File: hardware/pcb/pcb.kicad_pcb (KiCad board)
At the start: 2 copper layers, 26.7 x 56.6 mm, 32 parts, among them J1 L_GPIO, J2 R_GPIO, J3 USB_C_Receptacle_USB2.0_14P, U1 ESP32-C3-WROOM-02, U3 TPS62291

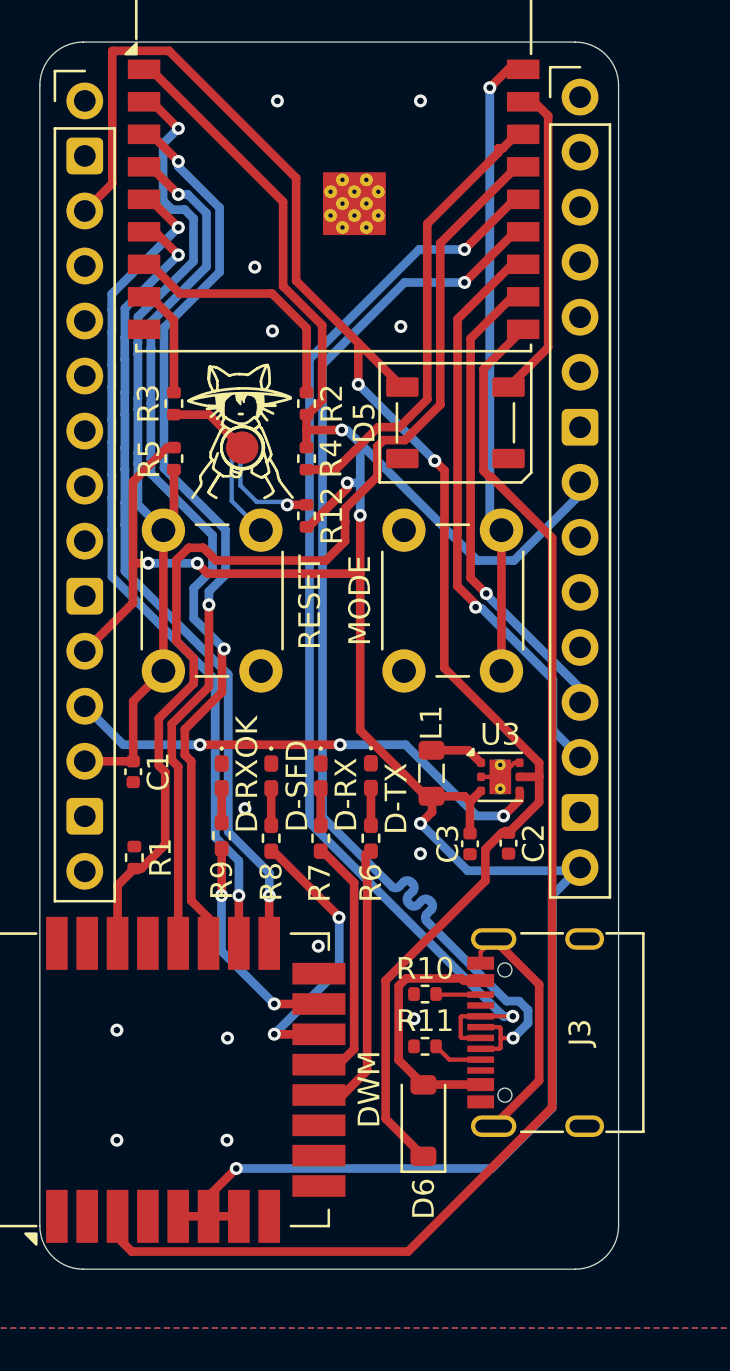
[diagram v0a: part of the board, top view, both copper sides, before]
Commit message: PCB: add some silkscreen art and transparency edits
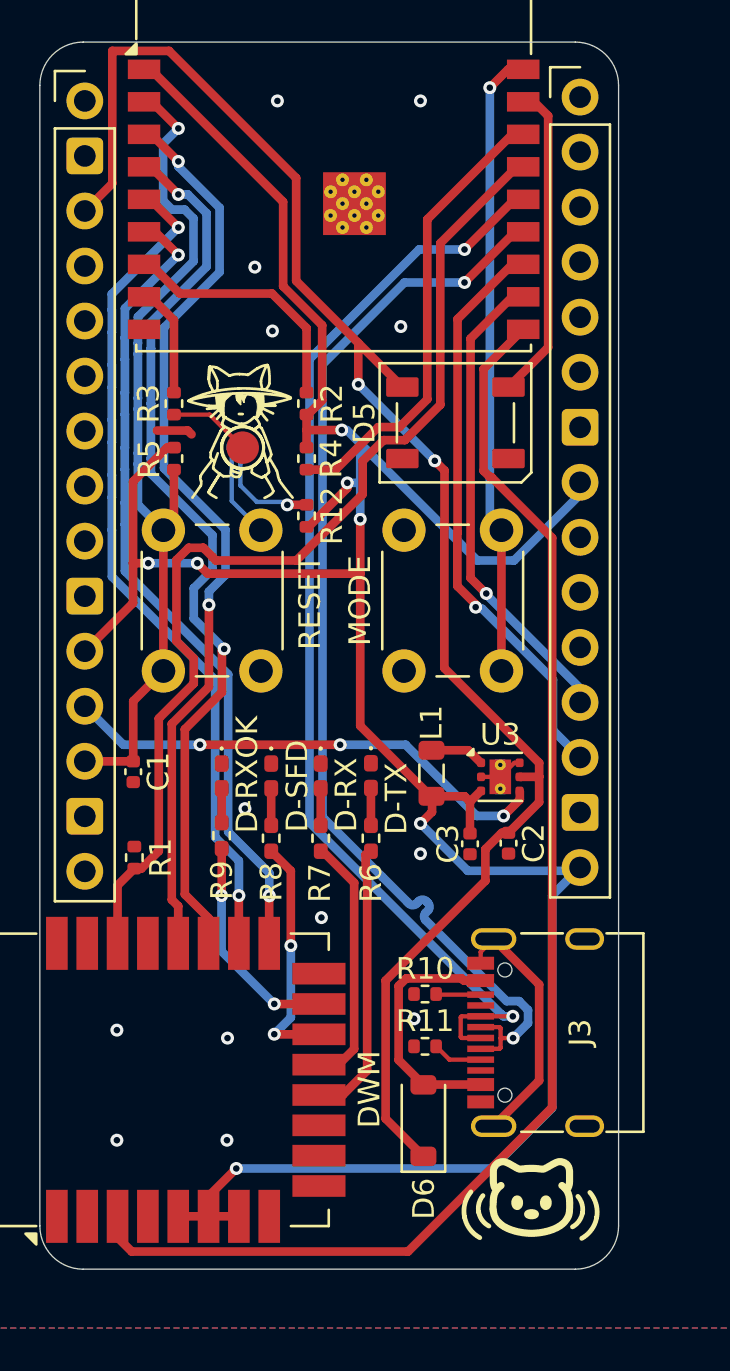
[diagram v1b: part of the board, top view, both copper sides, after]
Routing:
- net /SFDLED: track 13.1 -> 11.2 mm
- net GND: track 18.2 -> 19.9 mm
- net USB_D-: track 53.0 -> 51.6 mm
- net /U-IRQ: track 50.0 -> 48.9 mm

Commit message: Added IMU
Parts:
- removed BOOT1: TestPoint, TestPoint:TestPoint_Pad_D1.5mm
- removed C2, C3: 10uF, Capacitor_SMD:C_0402_1005Metric
- removed D-RX1: RXLED, LED_SMD:LED_0402_1005Metric_Pad0.77x0.64mm_HandSolder
- removed D-RXOK1: RXOKLED, LED_SMD:LED_0402_1005Metric_Pad0.77x0.64mm_HandSolder
- removed D-SFD1: SFDLED, LED_SMD:LED_0402_1005Metric_Pad0.77x0.64mm_HandSolder
- removed D-TX1: TXLED, LED_SMD:LED_0402_1005Metric_Pad0.77x0.64mm_HandSolder
- removed D1: LED, LED_SMD:LED_0201_0603Metric_Pad0.64x0.40mm_HandSolder
- removed D6: D_shottky, Diode_SMD:D_SOD-123
- removed DWM1: DWM1000, RF_Module:DWM1000
- removed J1: L_GPIO, Connector_PinHeader_2.54mm:PinHeader_1x15_P2.54mm_Vertical
- removed J2: R_GPIO, Connector_PinHeader_2.54mm:PinHeader_1x15_P2.54mm_Vertical
- removed J3: USB_C_Receptacle_USB2.0_14P, Connector_USB:USB_C_Receptacle_G-Switch_GT-USB-7010ASV
- removed L1: 2.2uH 1.2A, Inductor_SMD:L_0805_2012Metric
- removed R11: 5.1k, Resistor_SMD:R_0402_1005Metric
- removed R12: R, Resistor_SMD:R_0402_1005Metric
- removed R2, R3, R4: 10k, Resistor_SMD:R_0402_1005Metric
- removed R6, R7, R8, R9: R_Small, Resistor_SMD:R_0402_1005Metric_Pad0.72x0.64mm_HandSolder
- removed U3: TPS62291, Package_SON:WSON-6-1EP_2x2mm_P0.65mm_EP1x1.6mm_ThermalVias
- added A1: RaspberryPi_Pico_W, Module:RaspberryPi_Pico_Common_Unspecified, F.Cu at (124.5, 84.5)
- added DWM2: DWM3000, RF_Module:DWM1000, F.Cu at (201.2, 95.8)
- R10: value 5.1k -> IDK
- U1: value ESP32-C3-WROOM-02 -> BNO055; footprint RF_Module:ESP32-C3-WROOM-02 -> Package_LGA:LGA-28_5.2x3.8mm_P0.5mm
- moved C1 100.1 mm to (184.7, 41.0), turned to 0 degrees
- moved MODE1 96.8 mm to (182.4, 18.4), turned to 0 degrees
- moved RESET1 94.1 mm to (182.4, 26.9), turned to 0 degrees
- moved R5 89.9 mm to (181.8, 43.0), turned to 0 degrees
- moved U1 85.0 mm to (187.5, 65.1)
- moved D5 81.5 mm to (184.4, 36.7)
- moved R1 51.2 mm to (138.0, 61.0), turned to 0 degrees
- moved R10 41.7 mm to (138.0, 65.0)
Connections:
- R1 pad 1: /U-IRQ -> /UWB-IRQ
- R10 pad 1: GND -> Net-(DWM2-WAKEUP)
- R10 pad 2: Net-(J3-CC2) -> GND
- U1 pad 1: +3V3 -> unconnected-(U1-PIN1-Pad1)
- U1 pad 10: /U-RSTn -> /IMU-BL_IND
- U1 pad 11: /RXD -> /IMU-nRESET
- U1 pad 12: /TXD -> unconnected-(U1-PIN12-Pad12)
- U1 pad 13: USB_D- -> unconnected-(U1-PIN13-Pad13)
- U1 pad 14: USB_D+ -> /IMU-INT
- U1 pad 15: /U-IRQ -> unconnected-(U1-PIN15-Pad15)
- U1 pad 16: Net-(U1-IO2) -> unconnected-(U1-PIN16-Pad16)
- U1 pad 17: /LED -> /IMU-I2C_ADDR_SEL
- U1 pad 18: /BUTTON -> GND
- U1 pad 19: GND -> /IMU-SCL
- U1 pad 2: /ENABLE -> GND
- U1 pad 3: /U-SPICLK -> +3V3
- U1 pad 4: /U-SPIMISO -> /IMU-nBOOT_LOAD_PIN
- U1 pad 5: /U-SPIMOSI -> GND
- U1 pad 6: /U-SPICSn -> GND
- U1 pad 7: Net-(U1-IO8) -> unconnected-(U1-PIN7-Pad7)
- U1 pad 8: Net-(U1-IO9) -> unconnected-(U1-PIN8-Pad8)
- U1 pad 9: GND -> Net-(U1-CAP)
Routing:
- net +3V3: track 128.3 -> 0.00 mm, vias 7 -> 0
- net +5V: track 76.3 -> 0.00 mm, vias 2 -> 0
- net /U-RSTn: track 62.1 -> 0.00 mm
- net USB_D+: track 51.7 -> 0.00 mm, vias 2 -> 0
- net USB_D-: track 51.6 -> 0.00 mm, vias 2 -> 0
- net /U-IRQ: track 48.9 -> 0.00 mm
- net /U-SPICLK: track 42.4 -> 0.00 mm, vias 2 -> 0
- net /U-SPIMISO: track 42.0 -> 0.00 mm, vias 2 -> 0
- net /ENABLE: track 40.4 -> 0.00 mm, vias 1 -> 0
- net /U-SPIMOSI: track 38.9 -> 0.00 mm, vias 2 -> 0
- net /U-SPICSn: track 37.6 -> 0.00 mm, vias 2 -> 0
- net /BUTTON: track 29.0 -> 0.00 mm, vias 1 -> 0
- net /TXD: track 26.8 -> 0.00 mm, vias 1 -> 0
- net /SD-EN: track 22.9 -> 0.00 mm, vias 3 -> 0
- net /RXD: track 22.1 -> 0.00 mm, vias 1 -> 0
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- removed copper zone on B.Cu, net GND
- removed copper zone on F.Cu, net GND
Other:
- board outline removed
- board text removed: "D-RX"
- board text removed: "D-RXOK"
- board text removed: "D-SFD"
- board text removed: "D-TX"
- board text removed: "DWM"
- board text removed: "MODE"
- board text removed: "RESET"

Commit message: progress :)
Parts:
- added J1: Micro_SD_Card, Connector_Card:microSD_HC_Molex_47219-2001, F.Cu at (7.88, 7.53)
